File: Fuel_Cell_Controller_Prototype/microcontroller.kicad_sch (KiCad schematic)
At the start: 37 parts, among them J1 USB_OTG, J2 ST-LINK/V2, SW1 SW_MEC_5E, U1 STM32F746ZGTx, Y1 NX3225GD-8MHZ-EXS00A-CG04874

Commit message: update
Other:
- note added: "Buses for each bank of pins for intersheet access"
- note removed: "Bank Pin Buses for access"
- note removed: "USB FS"
- moved on the sheet: C1, C10, C11, C12, C13, C14, C17, C18, C2, C20, C21, C3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

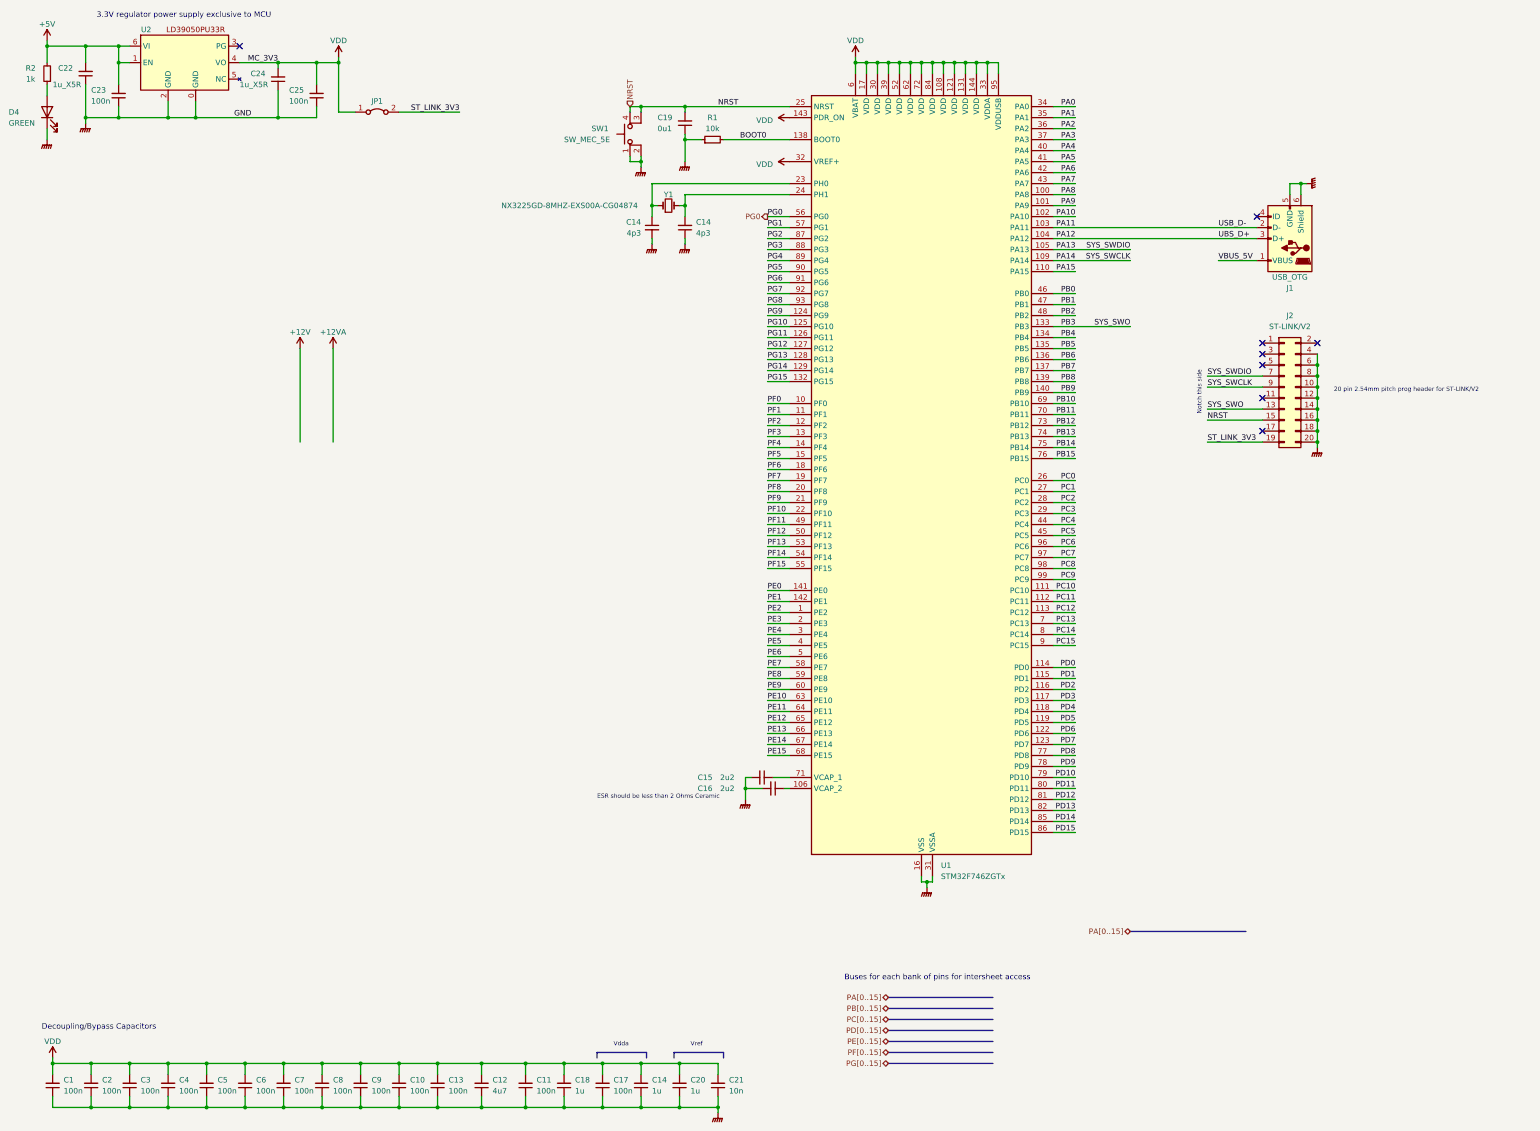
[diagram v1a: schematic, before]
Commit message: Added 6POS Molex connectors and started implementation of eFuses for 12v and 5V protection
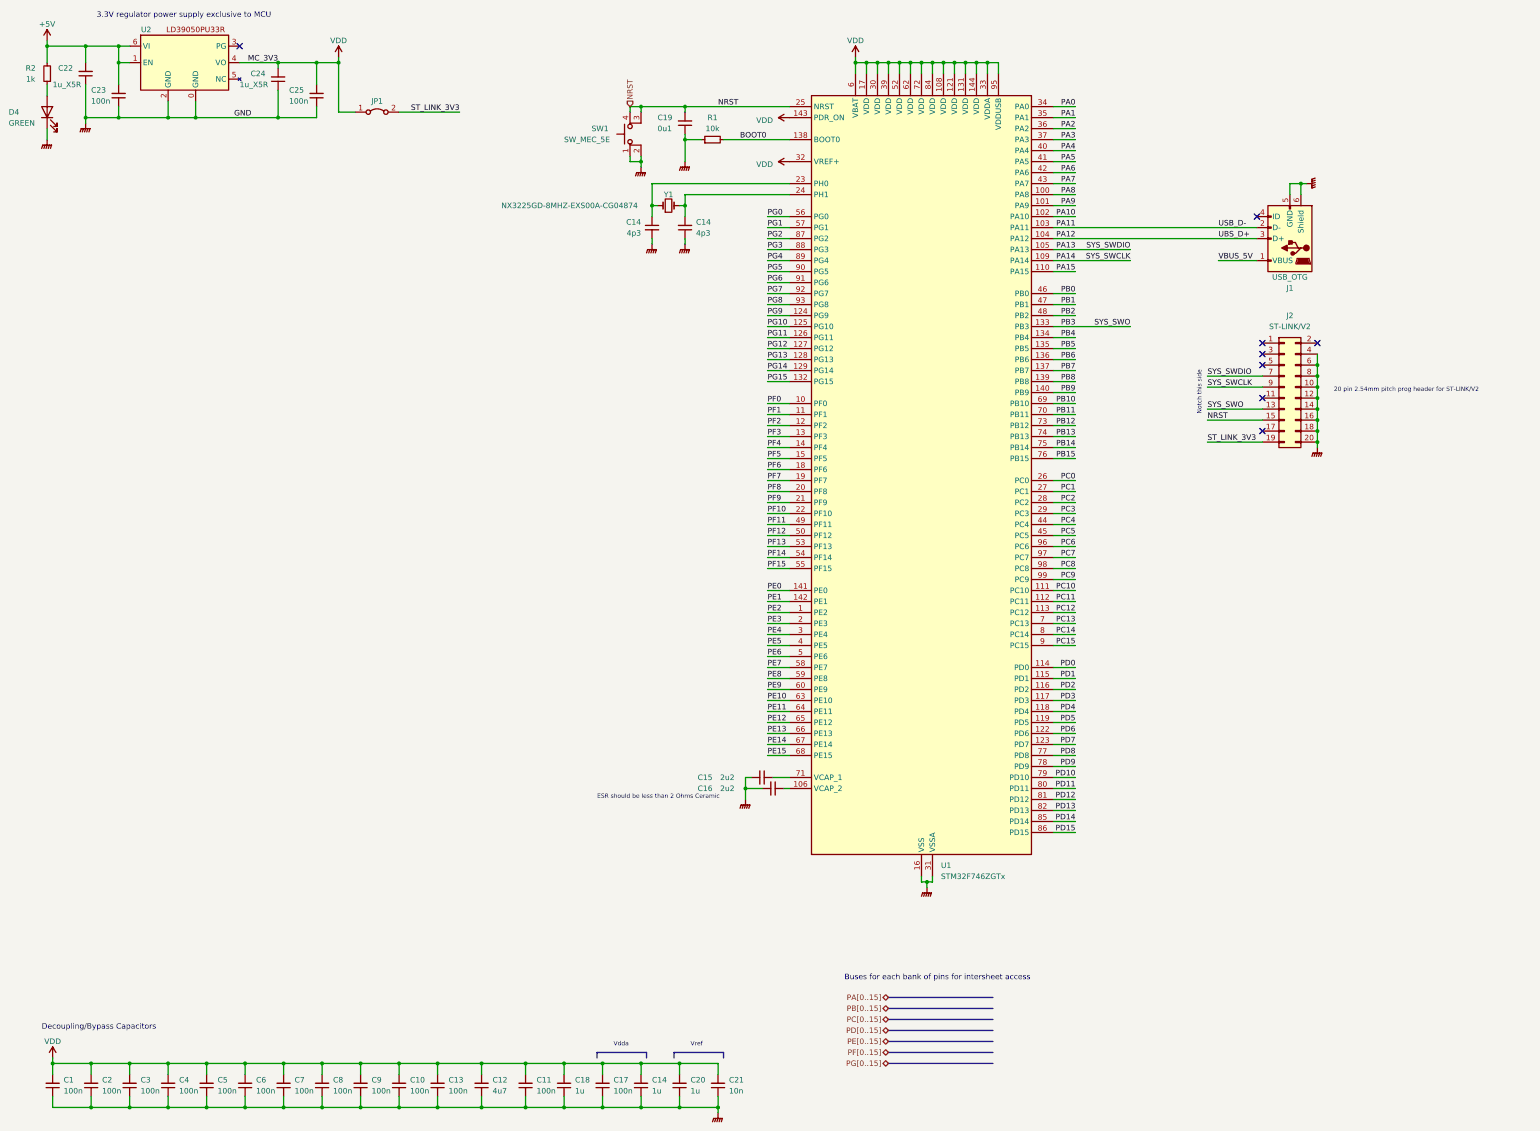
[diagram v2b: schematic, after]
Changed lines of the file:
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@@
     (stroke (width 0) (type default))
   )
-  (wire (pts (xy 95.25 99.06) (xy 95.25 120.65))
-    (stroke (width 0) (type default))
-  )
   (wire (pts (xy 38.1 45.72) (xy 45.72 45.72))
     (stroke (width 0) (type default))
@@
     (stroke (width 0) (type default))
   )
-  (wire (pts (xy 87.63 99.06) (xy 87.63 120.65))
-    (stroke (width 0) (type default))
-  )
   (wire (pts (xy 266.7 58.42) (xy 261.62 58.42))
     (stroke (width 0) (type default))
@@
     (stroke (width 0) (type default))
   )
-  (bus (pts (xy 279.4 233.68) (xy 306.07 233.68))
-    (stroke (width 0) (type default))
-  )
   (wire (pts (xy 266.7 210.82) (xy 261.62 210.82))
     (stroke (width 0) (type default))
@@
     (effects (font (size 1.27 1.27)) (justify right))
   )
-  (hierarchical_label "PA[0..15]" (shape bidirectional) (at 279.4 233.68 180) (fields_autoplaced)
-    (effects (font (size 1.27 1.27)) (justify right))
-  )
   (hierarchical_label "PG[0..15]" (shape bidirectional) (at 223.52 264.16 180) (fields_autoplaced)
     (effects (font (size 1.27 1.27)) (justify right))
@@
     (effects (font (size 1.27 1.27)) (justify right))
   )
-  (hierarchical_label "PG0" (shape output) (at 195.58 68.58 180) (fields_autoplaced)
-    (effects (font (size 1.27 1.27)) (justify right))
-  )
   (hierarchical_label "PF[0..15]" (shape bidirectional) (at 223.52 261.62 180) (fields_autoplaced)
     (effects (font (size 1.27 1.27)) (justify right))
@@
     )
   )
-  (symbol (lib_id "power:+12V") (at 87.63 99.06 0) (unit 1)
-    (in_bom yes) (on_board yes) (dnp no) (fields_autoplaced)
-    (property "Reference" "#PWR021" (at 87.63 102.87 0)
-      (effects (font (size 1.27 1.27)) hide)
-    )
-    (property "Value" "+12V" (at 87.63 95.25 0)
-      (effects (font (size 1.27 1.27)))
-    )
-    (property "Footprint" "" (at 87.63 99.06 0)
-      (effects (font (size 1.27 1.27)) hide)
-    )
-    (property "Datasheet" "" (at 87.63 99.06 0)
-      (effects (font (size 1.27 1.27)) hide)
-    )
-    (pin "1")
-    (instances
-      (project "Fuel_Cell_Controller_Prototype"
-        (path "/f651cec9-411c-4a4e-a163-5c49adbe6a12/c91aab04-72d2-4e29-8a0b-0fb415eded55"
-          (reference "#PWR021") (unit 1)
-        )
-      )
-    )
-  )
   (symbol (lib_id "Device:C_Small") (at 184.15 269.24 180) (unit 1)
     (in_bom yes) (on_board yes) (dnp no)
@@
         )
       )
-    )
-  )
-  (symbol (lib_id "power:+12VA") (at 95.25 99.06 0) (unit 1)
-    (in_bom yes) (on_board yes) (dnp no) (fields_autoplaced)
-    (property "Reference" "#PWR022" (at 95.25 102.87 0)
-      (effects (font (size 1.27 1.27)) hide)
-    )
-    (property "Value" "+12VA" (at 95.25 95.25 0)
-      (effects (font (size 1.27 1.27)))
-    )
-    (property "Footprint" "" (at 95.25 99.06 0)
-      (effects (font (size 1.27 1.27)) hide)
-    )
-    (property "Datasheet" "" (at 95.25 99.06 0)
-      (effects (font (size 1.27 1.27)) hide)
-    )
-    (pin "1")
-    (instances
-      (project "Fuel_Cell_Controller_Prototype"
-        (path "/f651cec9-411c-4a4e-a163-5c49adbe6a12/c91aab04-72d2-4e29-8a0b-0fb415eded55"
-          (reference "#PWR022") (unit 1)
-        )
-      )

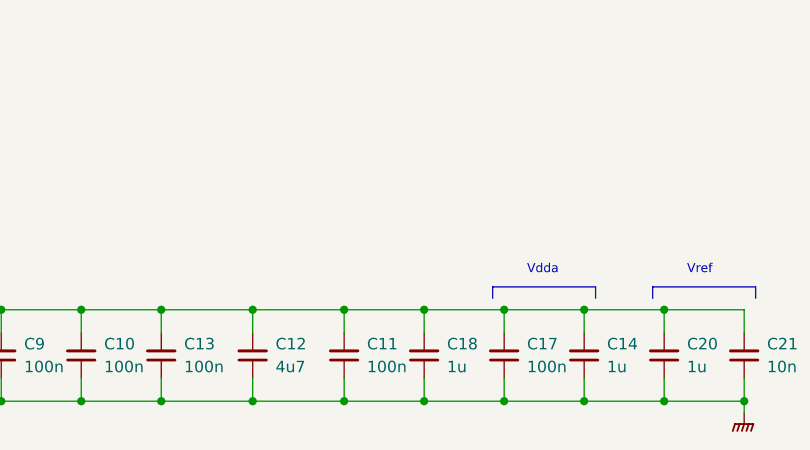
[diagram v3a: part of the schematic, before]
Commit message: Starting to add CAN infrastructure
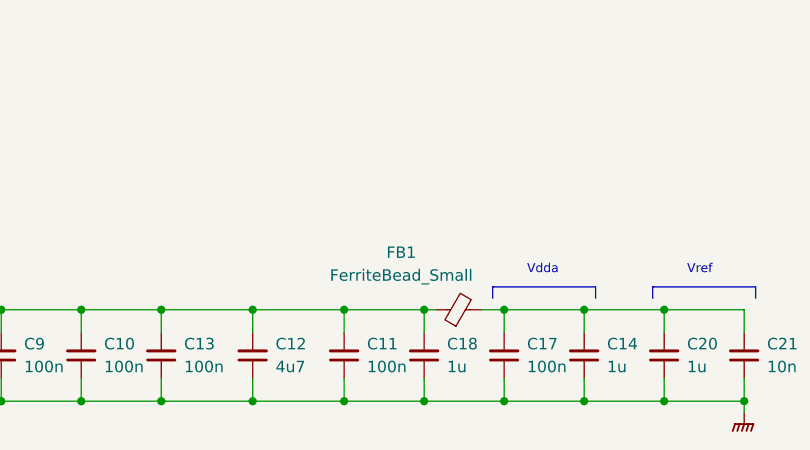
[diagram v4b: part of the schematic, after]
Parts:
- added FB1: FerriteBead_Small, symbol Device:FerriteBead_Small
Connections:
- net VDD: now also FB1.1; no longer C14.2, C17.2, C20.2, C21.2
- new net: C14.2, C17.2, C20.2, C21.2, FB1.2
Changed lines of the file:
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@@
   (junction (at 226.06 33.02) (diameter 0) (color 0 0 0 0)
   )
+  (junction (at 157.48 264.16) (diameter 0) (color 0 0 0 0)
+  )
   (junction (at 101.6 264.16) (diameter 0) (color 0 0 0 0)
   )
@@
   (junction (at 101.6 274.32) (diameter 0) (color 0 0 0 0)
   )
-  (junction (at 157.48 264.16) (diameter 0) (color 0 0 0 0)
-  )
   (junction (at 184.15 274.32) (diameter 0) (color 0 0 0 0)
   )
@@
   (junction (at 119.38 264.16) (diameter 0) (color 0 0 0 0)
   )
-  (junction (at 148.59 264.16) (diameter 0) (color 0 0 0 0)
-  )
   (junction (at 168.91 66.04) (diameter 0) (color 0 0 0 0)
   )
@@
   (junction (at 30.48 264.16) (diameter 0) (color 0 0 0 0)
   )
+  (junction (at 148.59 264.16) (diameter 0) (color 0 0 0 0)
+  )
   (junction (at 66.04 264.16) (diameter 0) (color 0 0 0 0)
   )
@@
     (stroke (width 0) (type default))
   )
+  (wire (pts (xy 148.59 264.16) (xy 149.86 264.16))
+    (stroke (width 0) (type default))
+  )
   (wire (pts (xy 243.84 33.02) (xy 246.38 33.02))
     (stroke (width 0) (type default))
@@
     (stroke (width 0) (type default))
   )
-  (wire (pts (xy 148.59 264.16) (xy 157.48 264.16))
-    (stroke (width 0) (type default))
-  )
   (wire (pts (xy 261.62 73.66) (xy 308.61 73.66))
     (stroke (width 0) (type default))
@@
     (stroke (width 0) (type default))
   )
+  (wire (pts (xy 154.94 264.16) (xy 157.48 264.16))
+    (stroke (width 0) (type default))
+  )
   (wire (pts (xy 195.58 111.76) (xy 200.66 111.76))
     (stroke (width 0) (type default))
@@
         )
       )
+    )
+  )
+  (symbol (lib_id "Device:FerriteBead_Small") (at 152.4 264.16 90) (unit 1)
+    (in_bom yes) (on_board yes) (dnp no)
+    (property "Reference" "FB1" (at 146.05 257.81 90)
+      (effects (font (size 1.27 1.27)))
+    )
+    (property "Value" "FerriteBead_Small" (at 146.05 260.35 90)
+      (effects (font (size 1.27 1.27)))
+    )
+    (property "Footprint" "" (at 152.4 265.938 90)
+      (effects (font (size 1.27 1.27)) hide)
+    )
+    (property "Datasheet" "~" (at 152.4 264.16 0)
+      (effects (font (size 1.27 1.27)) hide)
+    )
+    (pin "1")
+    (pin "2")
+    (instances
+      (project "Fuel_Cell_Controller_Prototype"
+        (path "/f651cec9-411c-4a4e-a163-5c49adbe6a12/c91aab04-72d2-4e29-8a0b-0fb415eded55"
+          (reference "FB1") (unit 1)
+        )
+      )

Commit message: Updates
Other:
- title: (none) -> Microcontroller
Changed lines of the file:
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@@
 (kicad_sch (version 20230121) (generator eeschema)
   (paper "A3")
+  (title_block
+    (title "Microcontroller")
+  )
   (junction (at 119.38 274.32) (diameter 0) (color 0 0 0 0)
   )

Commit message: Revert "huh"
This reverts commit 7bb3ffd8f300d735453e7bd9492734dd47e7a050.
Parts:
- removed C14: 1u, symbol Device:C_Small
- removed C17: 100n, symbol Device:C_Small
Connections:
- net VDD: no longer U1.32 (VREF+), U1.33 (VDDA), U1.6 (VBAT), U1.95 (VDDUSB)
- net VDDA: now reaches C20.2, C21.2, FB1.2
- net VDDA: now also U1.32 (VREF+), U1.33 (VDDA)
- net PB12 renamed CAN2_RX
- net PB13 renamed CAN2_TX
- net PB6 renamed I2C1_SCL
- net PB7 renamed I2C1_SDA
- net PF0 renamed 12V_REF_IN
- no-connect marks 8 -> 10
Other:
- note added: "Need to replace this clock with 25MHz"
- moved on the sheet: C20, C21

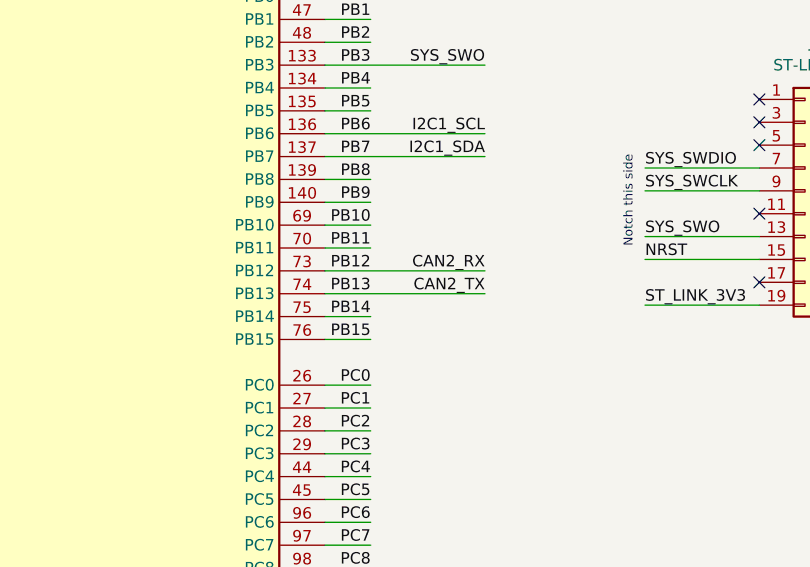
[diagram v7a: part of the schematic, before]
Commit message: Slight changes to CAN stuff
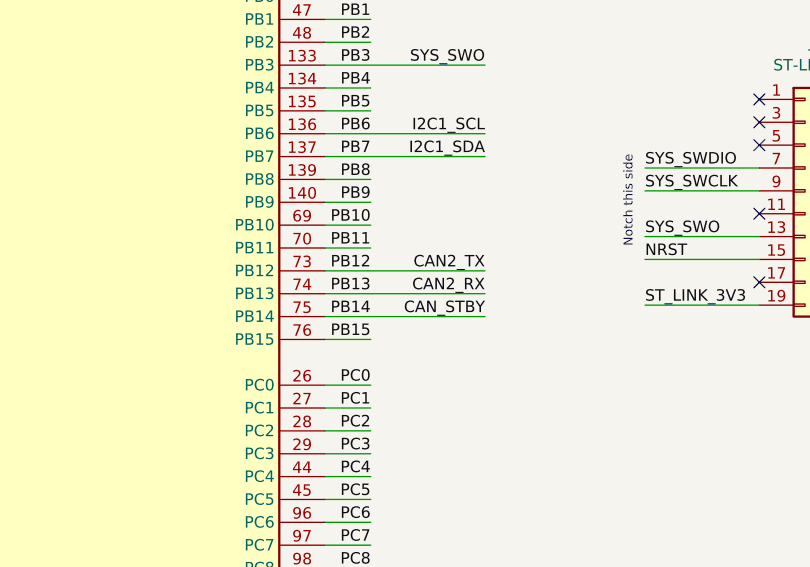
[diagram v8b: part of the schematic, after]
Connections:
- net CAN2_RX: now also U1.74 (PB13); no longer U1.73 (PB12)
- net CAN2_TX: now also U1.73 (PB12); no longer U1.74 (PB13)
- net PB14 renamed CAN_STBY
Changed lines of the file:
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@@
-    (stroke (width 0) (type default))
-  )
-  (wire (pts (xy 266.7 114.3) (xy 261.62 114.3))
     (stroke (width 0) (type default))
   )
@@
     (stroke (width 0) (type default))
   )
+  (wire (pts (xy 261.62 114.3) (xy 266.7 114.3))
+    (stroke (width 0) (type default))
+  )
   (wire (pts (xy 297.18 120.65) (xy 309.88 120.65))
     (stroke (width 0) (type default))
@@
     (stroke (width 0) (type default))
   )
+  (wire (pts (xy 261.62 121.92) (xy 279.4 121.92))
+    (stroke (width 0) (type default))
+  )
   (wire (pts (xy 38.1 45.72) (xy 45.72 45.72))
     (stroke (width 0) (type default))
@@
   )
   (wire (pts (xy 322.58 113.03) (xy 322.58 115.57))
-    (stroke (width 0) (type default))
-  )
-  (wire (pts (xy 266.7 121.92) (xy 261.62 121.92))
     (stroke (width 0) (type default))
   )
@@
     (effects (font (size 1.27 1.27)) (justify left bottom))
   )
-  (label "CAN2_TX" (at 279.4 119.38 180) (fields_autoplaced)
+  (label "CAN2_TX" (at 279.4 116.84 180) (fields_autoplaced)
     (effects (font (size 1.27 1.27)) (justify right bottom))
   )
@@
     (effects (font (size 1.27 1.27)) (justify right bottom))
   )
+  (label "CAN_STBY" (at 279.4 121.92 180) (fields_autoplaced)
+    (effects (font (size 1.27 1.27)) (justify right bottom))
+  )
   (label "PB7" (at 266.7 104.14 180) (fields_autoplaced)
     (effects (font (size 1.27 1.27)) (justify right bottom))
@@
     (effects (font (size 1.27 1.27)) (justify right bottom))
   )
-  (label "CAN2_RX" (at 279.4 116.84 180) (fields_autoplaced)
-    (effects (font (size 1.27 1.27)) (justify right bottom))
-  )
+  (label "CAN2_RX" (at 279.4 119.38 180) (fields_autoplaced)
+    (effects (font (size 1.27 1.27)) (justify right bottom))
+  )
